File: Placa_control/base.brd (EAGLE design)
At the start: 160 x 100 mm, 67 parts, among them Q10 IRF740, Q11 IRF740, Q5 IRF740, Q6 IRF740, Q7 IRF740, Q8 IRF740, Q9 IRF740

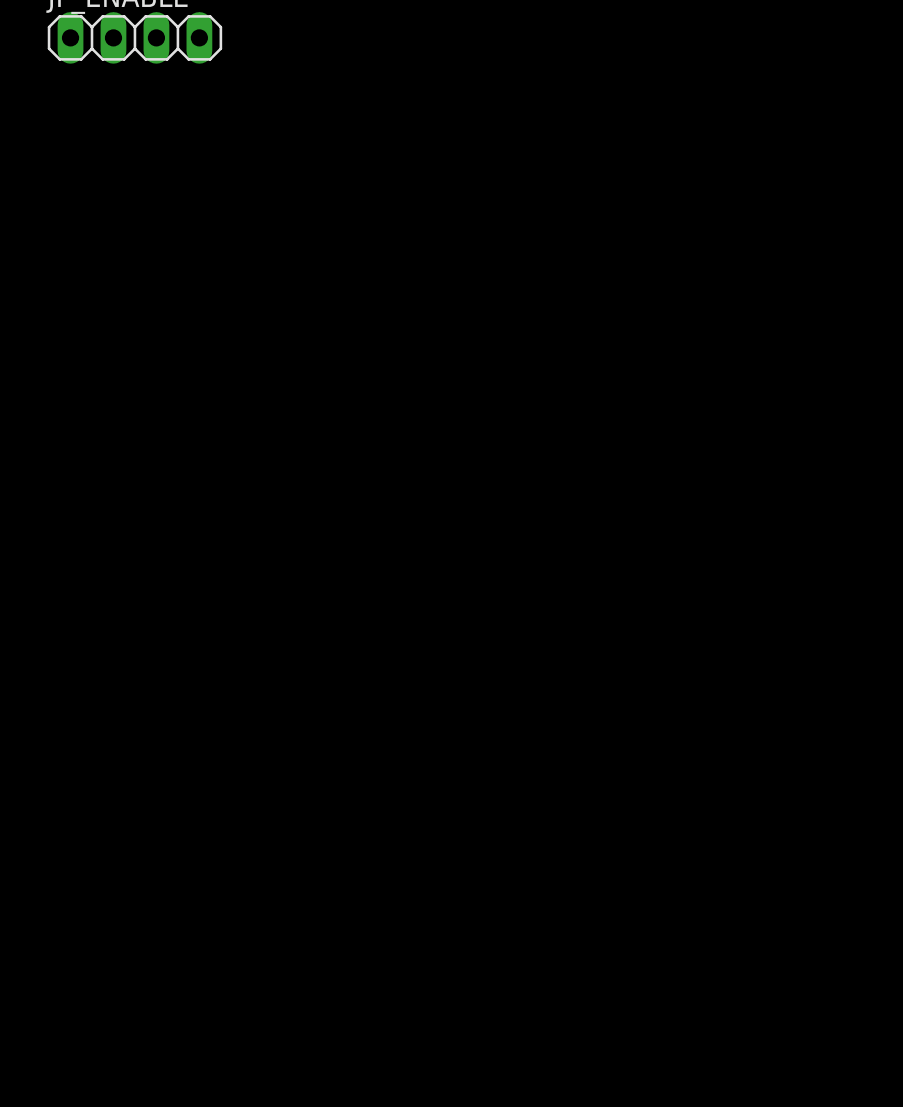
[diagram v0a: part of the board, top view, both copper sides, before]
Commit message: Actualizacion de la placa y codigo demo
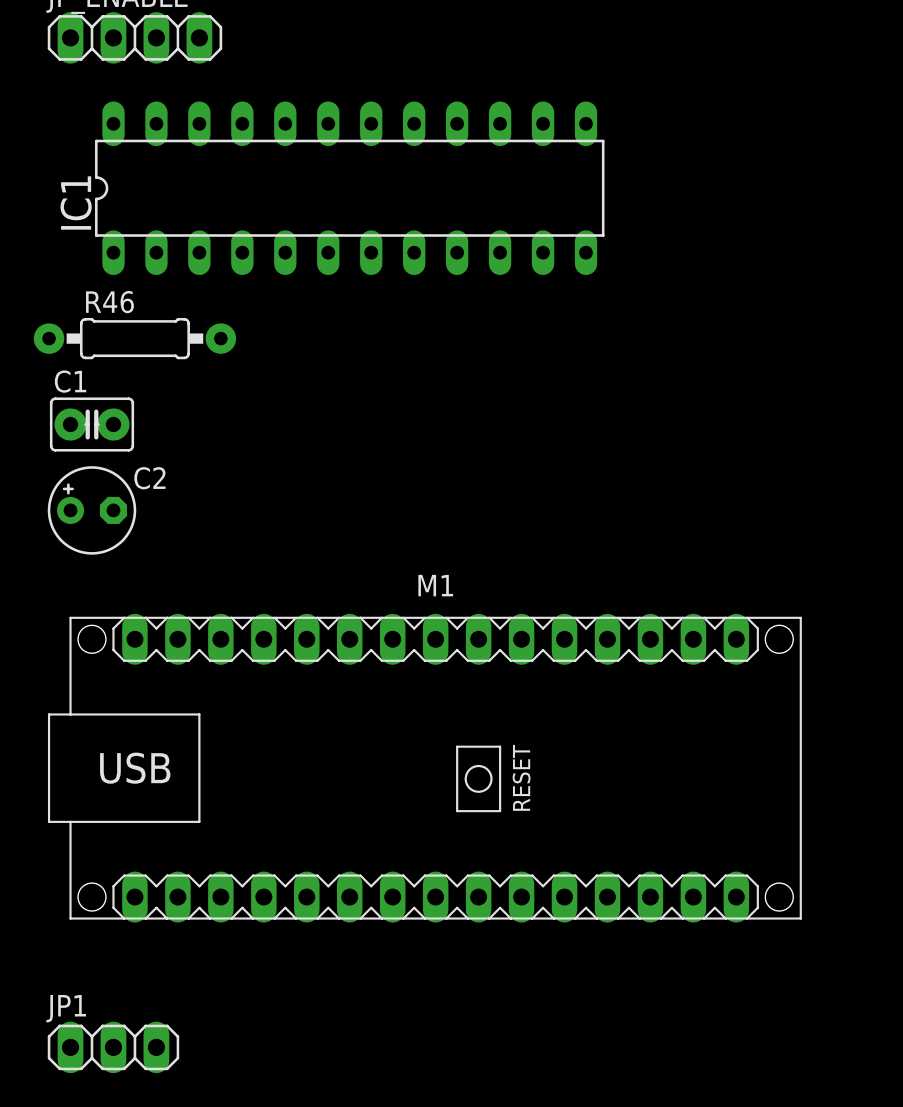
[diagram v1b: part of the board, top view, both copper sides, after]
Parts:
- added C1: (no value), rcl:C025-030X050
- added C2: (no value), rcl:E2,5-5
- added IC1: MAX7219CNG, maxim:DIL24-3
- added JP1: (no value), pinhead:1X03
- added M1: ARDUINO-NANO-3.0, diy-modules:ARDUINO-NANO-3.0
- added R46: 10k, rcl:0207/10
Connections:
- new net 3V3: M1.J2.14
- new net CLK: IC1.13, M1.J2.15
- new net CS: IC1.12, M1.J1.15
- new net MOSI: IC1.1, M1.J1.14
- new net N$15: IC1.18, R46.2
- new net N$21: JP1.1, M1.J2.1
- new net V_LOGIC: JP1.2, X1.2
- net 5V: now also C1.1, C2.+, IC1.19, JP1.3, M1.J2.4, R46.1; no longer X1.2
- net A_IN: now also IC1.14
- net B_IN: now also IC1.16
- net C_IN: now also IC1.20
- net D_IN: now also IC1.23
- net EN_1_IN: now also IC1.2
- net EN_2_IN: now also IC1.11
- net EN_3_IN: now also IC1.6
- net EN_4_IN: now also IC1.7
- net E_IN: now also IC1.21
- net F_IN: now also IC1.15
- net GND: now also C1.2, C2.-, IC1.4, IC1.9, M1.J1.4, M1.J2.2
- net G_IN: now also IC1.17
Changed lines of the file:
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@@
 <layer number="97" name="Info" color="7" fill="1" visible="no" active="no"/>
 <layer number="98" name="Guide" color="6" fill="1" visible="no" active="no"/>
+<layer number="101" name="Hidden" color="15" fill="1" visible="yes" active="yes"/>
+<layer number="102" name="Changes" color="12" fill="1" visible="yes" active="yes"/>
 </layers>
 <board>
@@
 <attribute name="VALUE" x="-62.23" y="-144.145" size="1.27" layer="27"/>
 </element>
+<element name="IC1" library="maxim" library_urn="urn:adsk.eagle:library:269" package="DIL24-3" package3d_urn="urn:adsk.eagle:package:3299/1" value="MAX7219CNG" x="-44.45" y="-149.86" smashed="yes">
+<attribute name="MF" value="MAXIM" x="-44.45" y="-149.86" size="1.778" layer="27" display="off"/>
+<attribute name="MPN" value="MAX7219CNG" x="-44.45" y="-149.86" size="1.778" layer="27" display="off"/>
+<attribute name="NAME" x="-59.7408" y="-152.527" size="1.778" layer="25" ratio="10" rot="R90"/>
+<attribute name="OC_FARNELL" value="1523914" x="-44.45" y="-149.86" size="1.778" layer="27" display="off"/>
+<attribute name="OC_NEWARK" value="34C4018" x="-44.45" y="-149.86" size="1.778" layer="27" display="off"/>
+<attribute name="VALUE" x="-57.912" y="-150.749" size="1.778" layer="27" ratio="10"/>
+</element>
+<element name="R46" library="rcl" package="0207/10" package3d_urn="urn:adsk.eagle:package:23491/1" value="10k" x="-57.15" y="-158.75" smashed="yes">
+<attribute name="NAME" x="-60.198" y="-157.226" size="1.27" layer="25" ratio="10"/>
+<attribute name="VALUE" x="-59.4106" y="-159.385" size="1.27" layer="27" ratio="10"/>
+</element>
+<element name="C1" library="rcl" package="C025-030X050" package3d_urn="urn:adsk.eagle:package:23631/1" value="" x="-59.69" y="-163.83" smashed="yes">
+<attribute name="NAME" x="-61.976" y="-161.925" size="1.27" layer="25" ratio="10"/>
+<attribute name="VALUE" x="-61.976" y="-166.878" size="1.27" layer="27" ratio="10"/>
+</element>
+<element name="C2" library="rcl" package="E2,5-5" package3d_urn="urn:adsk.eagle:package:23344/1" value="" x="-59.69" y="-168.91" smashed="yes">
+<attribute name="NAME" x="-57.277" y="-167.64" size="1.27" layer="25" ratio="10"/>
+<attribute name="VALUE" x="-57.277" y="-171.323" size="1.27" layer="27" ratio="10"/>
+</element>
+<element name="M1" library="diy-modules" package="ARDUINO-NANO-3.0" value="ARDUINO-NANO-3.0" x="-39.37" y="-184.15" smashed="yes">
+<attribute name="NAME" x="-39.37" y="-173.99" size="1.27" layer="25" align="bottom-center"/>
+<attribute name="VALUE" x="-39.37" y="-194.31" size="1.27" layer="27" align="top-center"/>
+</element>
+<element name="JP1" library="pinhead" library_urn="urn:adsk.eagle:library:325" package="1X03" package3d_urn="urn:adsk.eagle:package:22458/2" value="" x="-58.42" y="-200.66" smashed="yes">
+<attribute name="NAME" x="-62.3062" y="-198.8312" size="1.27" layer="25" ratio="10"/>
+<attribute name="VALUE" x="-62.23" y="-203.835" size="1.27" layer="27"/>
+</element>
 </elements>
 <signals>
@@
 <signal name="EN_2_IN">
 <contactref element="R1" pad="1"/>
+<contactref element="IC1" pad="11"/>
+<wire x1="-24.13" y1="25.4" x2="-33.02" y2="-153.67" width="0" layer="19" extent="1-1"/>
 </signal>
 <signal name="5V">
@@
 <contactref element="R28" pad="2"/>
 <contactref element="R34" pad="2"/>
-<contactref element="X1" pad="2"/>
-<wire x1="-26.67" y1="25.4" x2="-54.61" y2="-123.21" width="0" layer="19" extent="1-1"/>
+<contactref element="IC1" pad="19"/>
+<contactref element="R46" pad="1"/>
+<contactref element="C1" pad="1"/>
+<contactref element="C2" pad="+"/>
+<contactref element="M1" pad="J2.4"/>
+<contactref element="JP1" pad="3"/>
+<wire x1="-60.96" y1="-163.83" x2="-60.96" y2="-168.91" width="0" layer="19" extent="1-1"/>
+<wire x1="-62.23" y1="-158.75" x2="-60.96" y2="-163.83" width="0" layer="19" extent="1-1"/>
+<wire x1="-45.72" y1="-146.05" x2="-62.23" y2="-158.75" width="0" layer="19" extent="1-1"/>
+<wire x1="-55.88" y1="-200.66" x2="-60.96" y2="-168.91" width="0" layer="19" extent="1-1"/>
+<wire x1="-29.21" y1="-191.77" x2="-55.88" y2="-200.66" width="0" layer="19" extent="1-1"/>
+<wire x1="-26.67" y1="25.4" x2="-45.72" y2="-146.05" width="0" layer="19" extent="1-1"/>
 <wire x1="-26.67" y1="50.8" x2="-26.67" y2="25.4" width="0" layer="19" extent="1-1"/>
 <wire x1="-26.67" y1="66.04" x2="-26.67" y2="50.8" width="0" layer="19" extent="1-1"/>
@@
 <contactref element="R7" pad="1"/>
 <contactref element="X1" pad="3"/>
+<contactref element="IC1" pad="4"/>
+<contactref element="IC1" pad="9"/>
+<contactref element="C1" pad="2"/>
+<contactref element="C2" pad="-"/>
+<contactref element="M1" pad="J1.4"/>
+<contactref element="M1" pad="J2.2"/>
+<wire x1="-58.42" y1="-163.83" x2="-58.42" y2="-168.91" width="0" layer="19" extent="1-1"/>
+<wire x1="-50.8" y1="-153.67" x2="-58.42" y2="-163.83" width="0" layer="19" extent="1-1"/>
+<wire x1="-38.1" y1="-153.67" x2="-50.8" y2="-153.67" width="0" layer="19" extent="1-1"/>
+<wire x1="-29.21" y1="-176.53" x2="-38.1" y2="-153.67" width="0" layer="19" extent="1-1"/>
+<wire x1="-24.13" y1="-191.77" x2="-29.21" y2="-176.53" width="0" layer="19" extent="1-1"/>
+<wire x1="-49.61" y1="-123.21" x2="-50.8" y2="-153.67" width="0" layer="19" extent="1-1"/>
 <wire x1="-54.61" y1="-55.88" x2="-49.61" y2="-123.21" width="0" layer="19" extent="1-1"/>
 <wire x1="-54.61" y1="-46.99" x2="-54.61" y2="-55.88" width="0" layer="19" extent="1-1"/>
@@
 <signal name="EN_1_IN">
 <contactref element="R21" pad="1"/>
+<contactref element="IC1" pad="2"/>
+<wire x1="-24.13" y1="50.8" x2="-55.88" y2="-153.67" width="0" layer="19" extent="1-1"/>
 </signal>
 <signal name="EN_1_OUT">
@@
 <signal name="EN_3_IN">
 <contactref element="R27" pad="1"/>
+<contactref element="IC1" pad="6"/>
+<wire x1="-49.53" y1="55.88" x2="-45.72" y2="-153.67" width="0" layer="19" extent="1-1"/>
 </signal>
 <signal name="EN_3_OUT">
@@
 <signal name="EN_4_IN">
 <contactref element="R33" pad="1"/>
+<contactref element="IC1" pad="7"/>
+<wire x1="-24.13" y1="66.04" x2="-43.18" y2="-153.67" width="0" layer="19" extent="1-1"/>
 </signal>
 <signal name="EN_4_OUT">
@@
 <contactref element="R15" pad="2"/>
 <contactref element="R39" pad="2"/>
+<contactref element="IC1" pad="21"/>
+<wire x1="-52.07" y1="-86.36" x2="-50.8" y2="-146.05" width="0" layer="19" extent="1-1"/>
 <wire x1="-39.37" y1="40.64" x2="-52.07" y2="-86.36" width="0" layer="19" extent="1-1"/>
 </signal>
@@
 <contactref element="R7" pad="2"/>
 <contactref element="R4" pad="2"/>
+<contactref element="IC1" pad="14"/>
+<wire x1="-52.07" y1="-66.04" x2="-33.02" y2="-146.05" width="0" layer="19" extent="1-1"/>
 <wire x1="-39.37" y1="30.48" x2="-52.07" y2="-66.04" width="0" layer="19" extent="1-1"/>
 </signal>
@@
 <contactref element="R9" pad="2"/>
 <contactref element="R24" pad="2"/>
+<contactref element="IC1" pad="16"/>
+<wire x1="-52.07" y1="-71.12" x2="-38.1" y2="-146.05" width="0" layer="19" extent="1-1"/>
 <wire x1="-13.97" y1="35.56" x2="-52.07" y2="-71.12" width="0" layer="19" extent="1-1"/>
 </signal>
@@
 <contactref element="R11" pad="2"/>
 <contactref element="R30" pad="2"/>
+<contactref element="IC1" pad="20"/>
+<wire x1="-52.07" y1="-76.2" x2="-48.26" y2="-146.05" width="0" layer="19" extent="1-1"/>
 <wire x1="-39.37" y1="35.56" x2="-52.07" y2="-76.2" width="0" layer="19" extent="1-1"/>
 </signal>
@@
 <contactref element="R13" pad="2"/>
 <contactref element="R36" pad="2"/>
+<contactref element="IC1" pad="23"/>
+<wire x1="-52.07" y1="-81.28" x2="-55.88" y2="-146.05" width="0" layer="19" extent="1-1"/>
 <wire x1="-13.97" y1="40.64" x2="-52.07" y2="-81.28" width="0" layer="19" extent="1-1"/>
 </signal>
@@
 <contactref element="R17" pad="2"/>
 <contactref element="R40" pad="2"/>
+<contactref element="IC1" pad="15"/>
+<wire x1="-52.07" y1="-91.44" x2="-35.56" y2="-146.05" width="0" layer="19" extent="1-1"/>
 <wire x1="-13.97" y1="45.72" x2="-52.07" y2="-91.44" width="0" layer="19" extent="1-1"/>
 </signal>
@@
 <contactref element="R19" pad="2"/>
 <contactref element="R41" pad="2"/>
+<contactref element="IC1" pad="17"/>
+<wire x1="-52.07" y1="-96.52" x2="-40.64" y2="-146.05" width="0" layer="19" extent="1-1"/>
 <wire x1="-39.37" y1="45.72" x2="-52.07" y2="-96.52" width="0" layer="19" extent="1-1"/>
 </signal>
@@
 <wire x1="49.53" y1="71.12" x2="-52.07" y2="-116.84" width="0" layer="19" extent="1-1"/>
 </signal>
+<signal name="CLK">
+<contactref element="IC1" pad="13"/>
+<contactref element="M1" pad="J2.15"/>
+<wire x1="-30.48" y1="-146.05" x2="-57.15" y2="-191.77" width="0" layer="19" extent="1-1"/>
+</signal>
+<signal name="CS">
+<contactref element="IC1" pad="12"/>
+<contactref element="M1" pad="J1.15"/>
+<wire x1="-30.48" y1="-153.67" x2="-57.15" y2="-176.53" width="0" layer="19" extent="1-1"/>
+</signal>
+<signal name="MOSI">
+<contactref element="IC1" pad="1"/>
+<contactref element="M1" pad="J1.14"/>
+<wire x1="-58.42" y1="-153.67" x2="-54.61" y2="-176.53" width="0" layer="19" extent="1-1"/>
+</signal>
+<signal name="N$15">
+<contactref element="IC1" pad="18"/>
+<contactref element="R46" pad="2"/>
+<wire x1="-43.18" y1="-146.05" x2="-52.07" y2="-158.75" width="0" layer="19" extent="1-1"/>
+</signal>
+<signal name="3V3">
+<contactref element="M1" pad="J2.14"/>
+</signal>
+<signal name="N$21">
+<contactref element="M1" pad="J2.1"/>
+<contactref element="JP1" pad="1"/>
+<wire x1="-60.96" y1="-200.66" x2="-21.59" y2="-191.77" width="0" layer="19" extent="1-1"/>
+</signal>
+<signal name="V_LOGIC">
+<contactref element="JP1" pad="2"/>
+<contactref element="X1" pad="2"/>
+<wire x1="-58.42" y1="-200.66" x2="-54.61" y2="-123.21" width="0" layer="19" extent="1-1"/>
+</signal>
 </signals>
